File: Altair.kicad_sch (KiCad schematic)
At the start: 14 parts, among them J1 Battery, J2 Battery, SW95 RST, SW97 RST, SW98 PWR, SW99 PWR, U1 nice_nano, U2 nice_nano

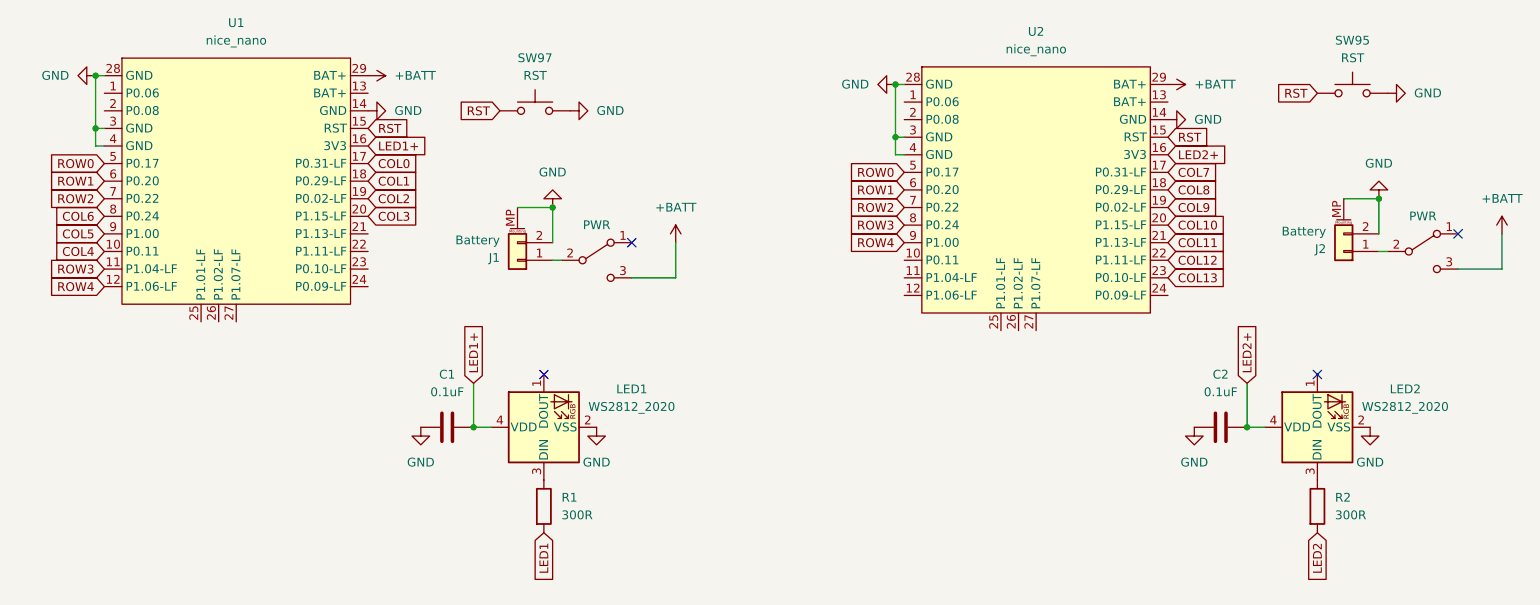
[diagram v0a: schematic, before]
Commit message: Remove Led
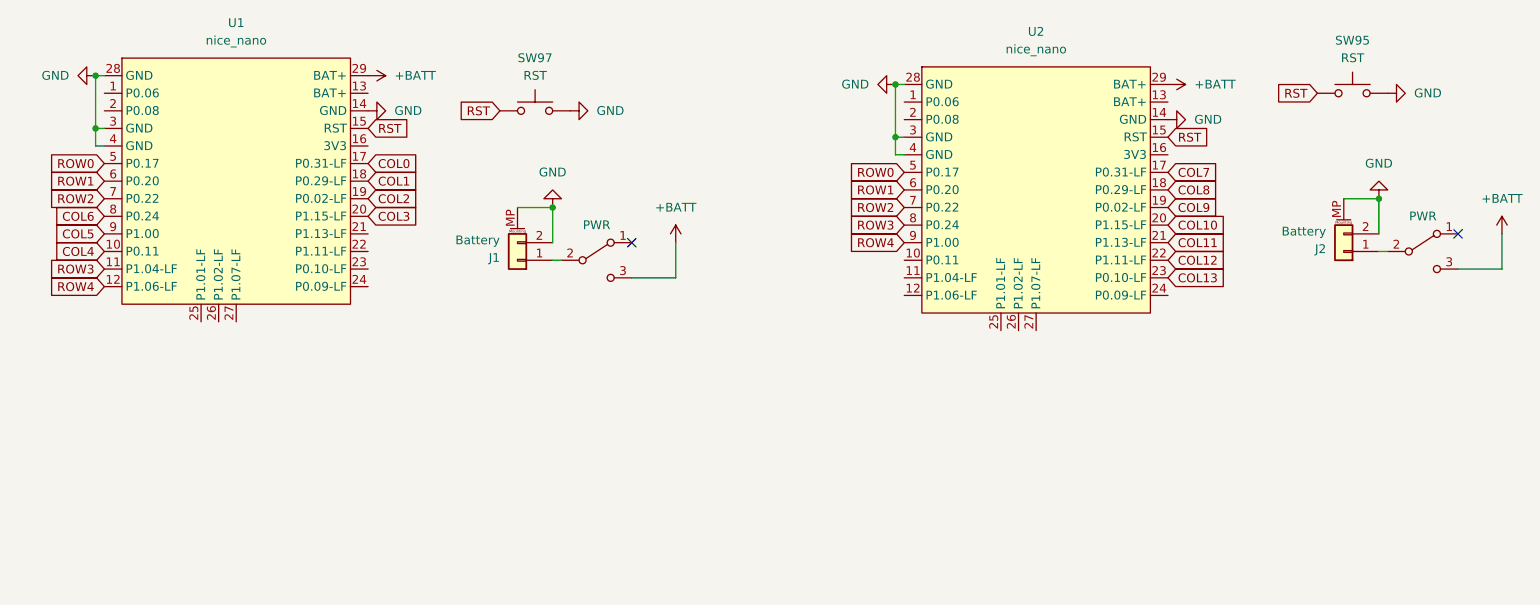
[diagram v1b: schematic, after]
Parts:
- removed C1, C2: 0.1uF, Capacitor_SMD:C_0805_2012Metric, symbol Device:C
- removed LED1, LED2: WS2812_2020, PCM_marbastlib-various:LED_WS2812_2020, symbol PCM_marbastlib-various:WS2812_2020
- removed R1, R2: 300R, Resistor_SMD:R_0815_2038Metric, symbol Device:R
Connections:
- net LED1+: no longer names the net of U1.16 (3V3)
- net LED2+: no longer names the net of U2.16 (3V3)
- no-connect marks 4 -> 2

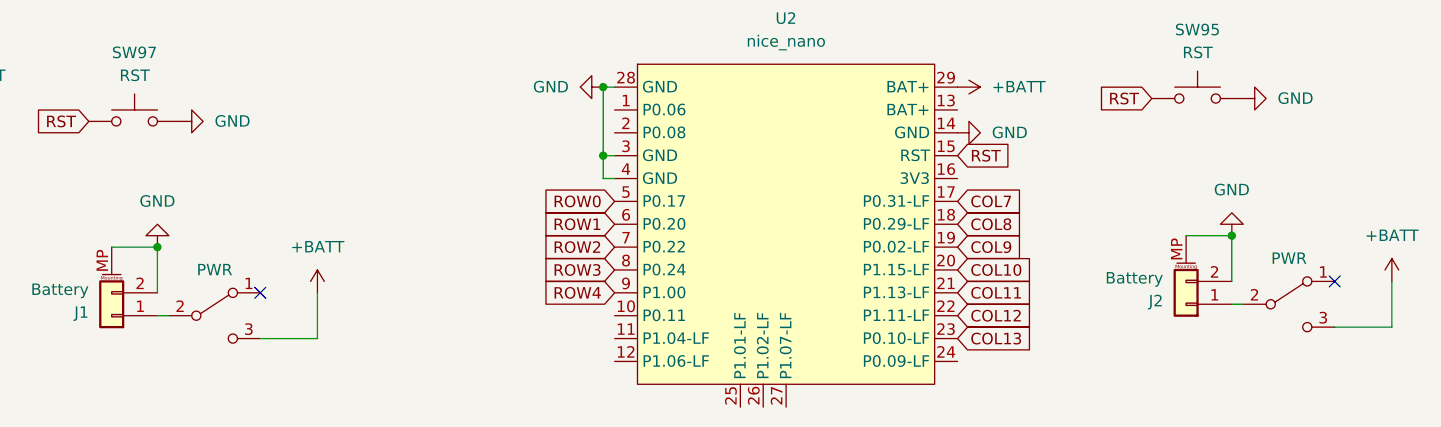
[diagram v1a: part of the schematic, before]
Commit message: Remove onoff button
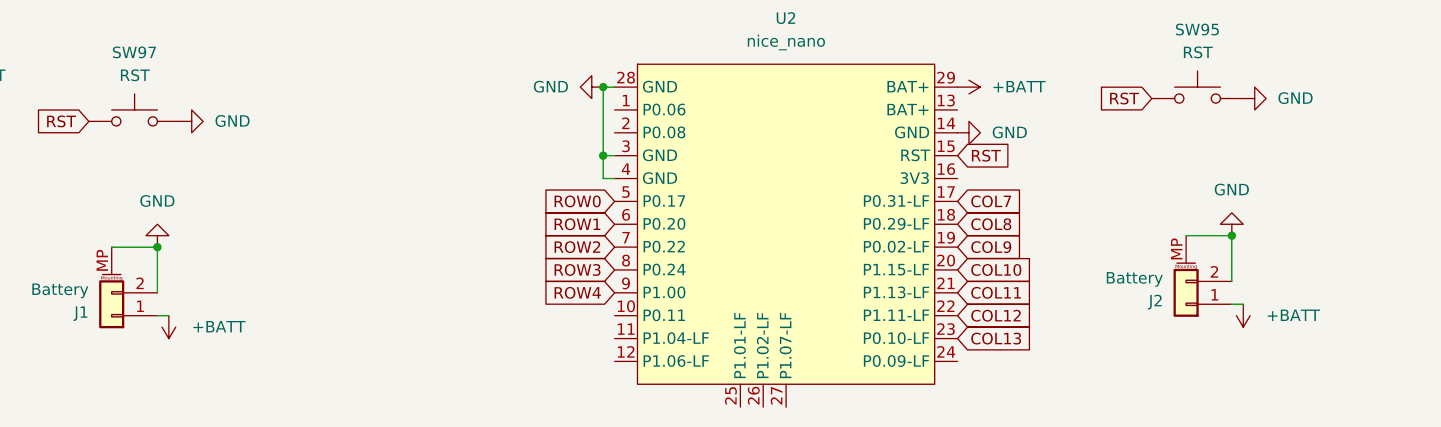
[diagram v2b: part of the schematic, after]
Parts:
- removed SW98, SW99: PWR, KLOTZ:MSK12C02_reversible, symbol Switch:SW_DPDT_x2
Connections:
- net +BATT: now also J1.1 (Pin_1), J2.1 (Pin_1)
- no-connect marks 2 -> 0

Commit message: Done routing for SW
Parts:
- removed J2: Battery, Connector_JST:JST_PH_S2B-PH-SM4-TB_1x02-1MP_P2.00mm_Horizontal, symbol Connector_Generic_MountingPin:Conn_01x02_MountingPin
- removed SW95, SW97: RST, PTS526_SMG15_SMTR2_LFS:SW_PTS526_SMG15_SMTR2_LFS, symbol Switch:SW_Push
- removed U2: nice_nano, PCM_marbastlib-xp-promicroish:nice_nano_AH_USBup, symbol PCM_marbastlib-promicroish:nice_nano
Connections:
- net ROW1: now also U1.7 (P0.22); no longer U1.6 (P0.20)
- net ROW2: now also U1.6 (P0.20); no longer U1.7 (P0.22)
- net ROW4: now also U1.24 (P0.09-LF); no longer U1.12 (P1.06-LF)

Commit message: Done for 1 side PCB
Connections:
- net +BATT: now also U1.13 (BAT+); no longer U1.29 (BAT+)
- net COL0: now also U1.18 (P0.29-LF); no longer U1.17 (P0.31-LF)
- net COL1: now also U1.17 (P0.31-LF); no longer U1.18 (P0.29-LF)
- net COL2: now also U1.16 (3V3); no longer U1.19 (P0.02-LF)
- net COL3: now also U1.19 (P0.02-LF); no longer U1.20 (P1.15-LF)
- net ROW1: now also U1.12 (P1.06-LF); no longer U1.7 (P0.22)
- net ROW2: now also U1.23 (P0.10-LF); no longer U1.6 (P0.20)

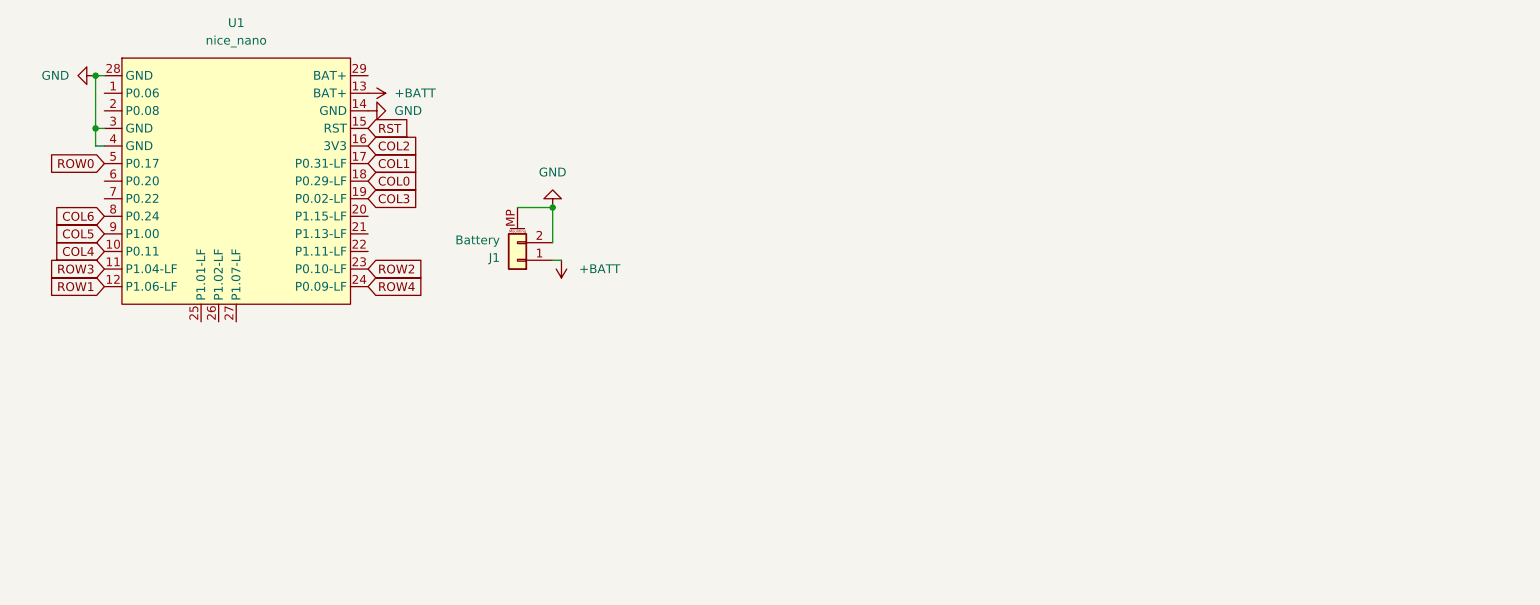
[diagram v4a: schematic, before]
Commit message: add 2 MCU
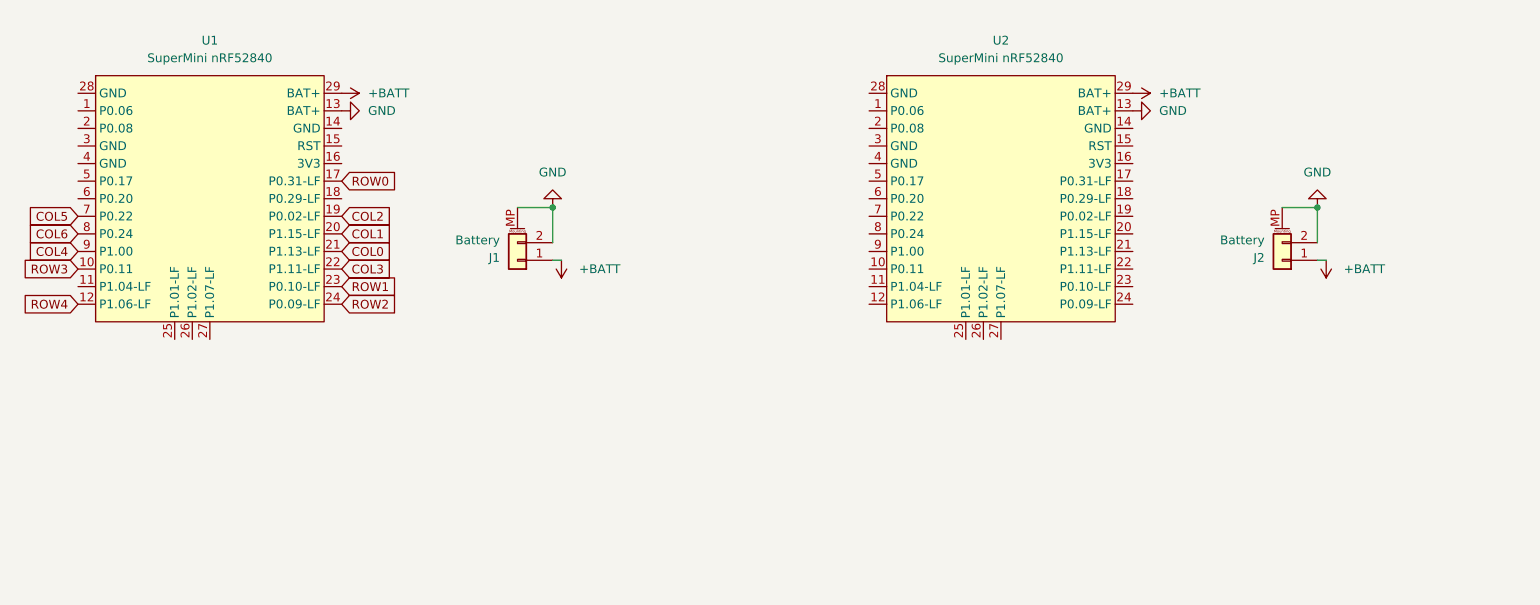
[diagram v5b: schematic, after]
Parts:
- removed U1: nice_nano, PCM_marbastlib-xp-promicroish:nice_nano_AH_USBup, symbol PCM_marbastlib-promicroish:nice_nano
- added J2: Battery, Connector_JST:JST_PH_S2B-PH-SM4-TB_1x02-1MP_P2.00mm_Horizontal, symbol Connector_Generic_MountingPin:Conn_01x02_MountingPin
- added U1, U2: SuperMini nRF52840, marbastlib-xp-promicroish:SuperMini_nRF52840_AH_USBdn, symbol marbastlib-promicroish:SuperMini_nRF52840
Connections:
- net +BATT: now also J2.1 (Pin_1), U1.29 (BAT+), U2.29 (BAT+)
- net COL0: now also U1.21 (P1.13-LF)
- net COL1: now also U1.20 (P1.15-LF)
- net COL2: now also U1.19 (P0.02-LF)
- net COL3: now also U1.22 (P1.11-LF)
- net COL4: now also U1.9 (P1.00)
- net COL5: now also U1.7 (P0.22)
- net COL6: now also U1.8 (P0.24)
- net GND: now also J2.2 (Pin_2), J2.MP (MountPin), U1.13 (BAT+), U2.13 (BAT+)
- net ROW0: now also U1.17 (P0.31-LF)
- net ROW1: now also U1.23 (P0.10-LF)
- net ROW2: now also U1.24 (P0.09-LF)
- net ROW3: now also U1.10 (P0.11)
- net ROW4: now also U1.12 (P1.06-LF)
